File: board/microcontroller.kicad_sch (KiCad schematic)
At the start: 1 part, among them U301 ATSAML21G18B-AUT

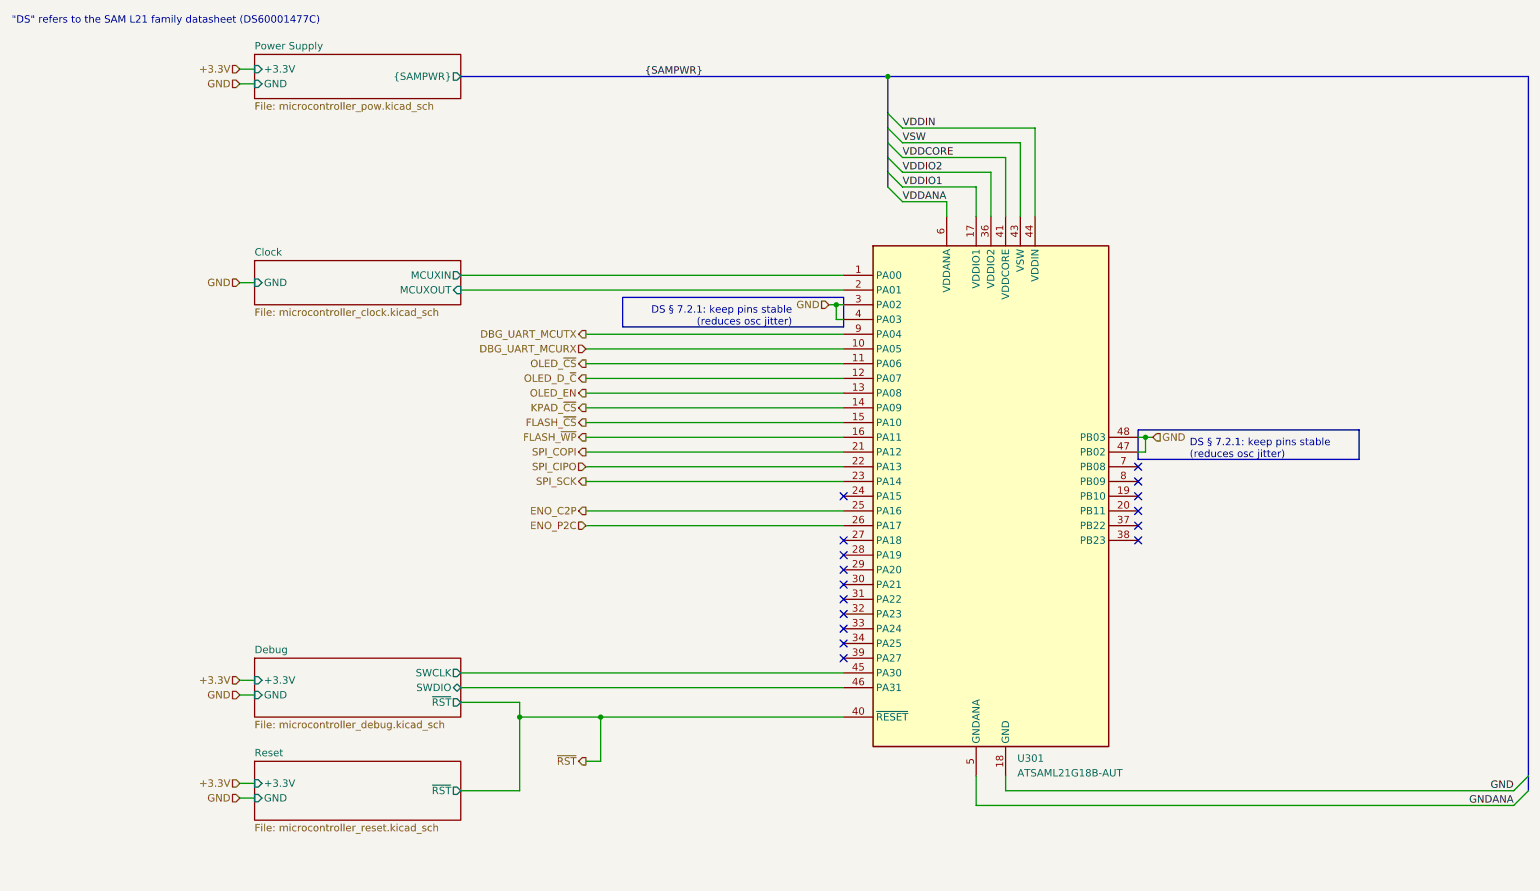
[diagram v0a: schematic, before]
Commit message: redo board with STM32G0B0CET
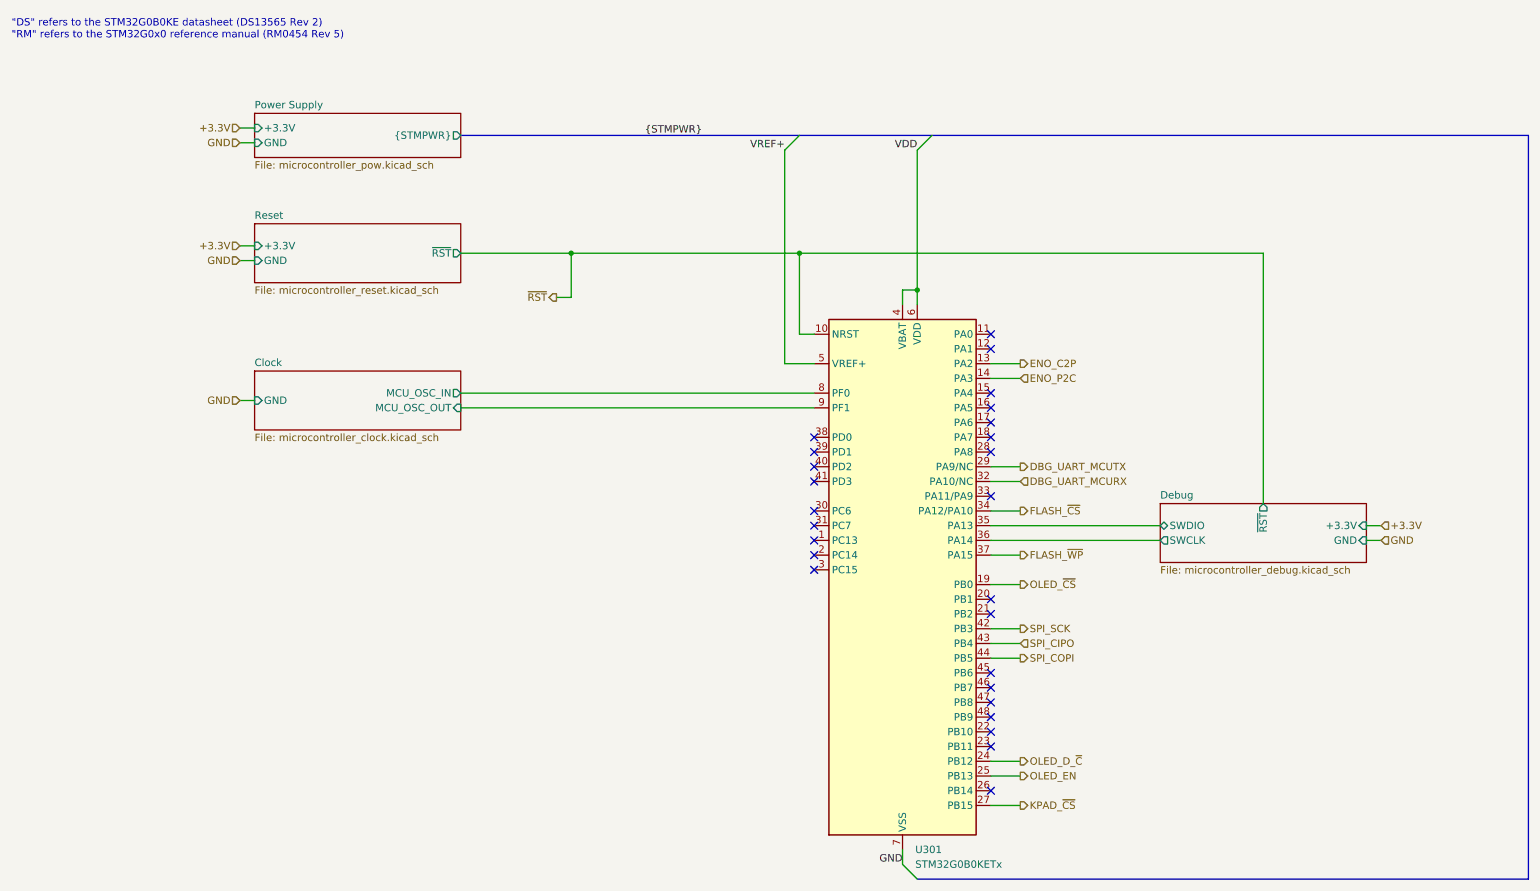
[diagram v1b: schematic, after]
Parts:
- removed U301: ATSAML21G18B-AUT, Package_QFP:TQFP-48_7x7mm_P0.5mm, symbol MCU_Microchip_SAML:ATSAML21G18B-AUT
- added U301: STM32G0B0KETx, Package_QFP:LQFP-48_7x7mm_P0.5mm, symbol MCU_ST_STM32G0:STM32G0B0CETx
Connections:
- net DBG_UART_MCURX: now also U301.32 (PA10/NC)
- net DBG_UART_MCUTX: now also U301.29 (PA9/NC)
- net Debug/SWCLK: now also U301.36 (PA14)
- net Debug/SWDIO: now also U301.35 (PA13)
- net ENO_C2P: now also U301.13 (PA2)
- net ENO_P2C: now also U301.14 (PA3)
- net FLASH_~{CS}: now also U301.34 (PA12/PA10)
- net FLASH_~{WP}: now also U301.37 (PA15)
- net GND: now also U301.7 (VSS)
- net KPAD_~{CS}: now also U301.27 (PB15)
- net OLED_D_~{C}: now also U301.24 (PB12)
- net OLED_EN: now also U301.25 (PB13)
- net OLED_~{CS}: now also U301.19 (PB0)
- net SPI_CIPO: now also U301.43 (PB4)
- net SPI_COPI: now also U301.44 (PB5)
- net SPI_SCK: now also U301.42 (PB3)
- net ~{RST}: now also U301.10 (NRST)
- new net Clock/MCU_OSC_IN: U301.8 (PF0)
- new net Clock/MCU_OSC_OUT: U301.9 (PF1)
- new net VDD: U301.4 (VBAT), U301.6 (VDD)
- new net VREF+: U301.5 (VREF+)
- no-connect marks 16 -> 26
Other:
- sheet Clock ports: added MCU_OSC_IN, MCU_OSC_OUT; removed MCUXIN, MCUXOUT
- sheet Power Supply ports: added {STMPWR}; removed {SAMPWR}
- note added: ""DS" refers to the STM32G0B0KE datasheet (DS13565 Rev 2) "RM" refers to the STM32G0x0 reference manual (RM0454 Rev 5)"
- note removed: ""DS" refers to the SAM L21 family datasheet (DS60001477C)"
- note removed: "DS § 7.2.1: keep pins stable (reduces osc jitter)"
